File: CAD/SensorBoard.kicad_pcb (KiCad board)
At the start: 4 copper layers, 69.9 x 40 mm, 82 parts, among them J1 USB C 2.0, J2 SWD Connector, J3 UART Connector, J4 DAC Connector, M1 M1, M2 M2, M3 M3, M4 M4, SW1 SW_1, SW2 SW_2, SW3 SW_3, SW4 SW_4, SW5 SW_BOOT, SW6 SW_RST, U1 STM32U073CCT6, U2 MIC5365, U3 USBLC6-2SC6, U4 BME680, U5 BMI323, U6 TC1047, X1 32MHz, X2 32kHz768

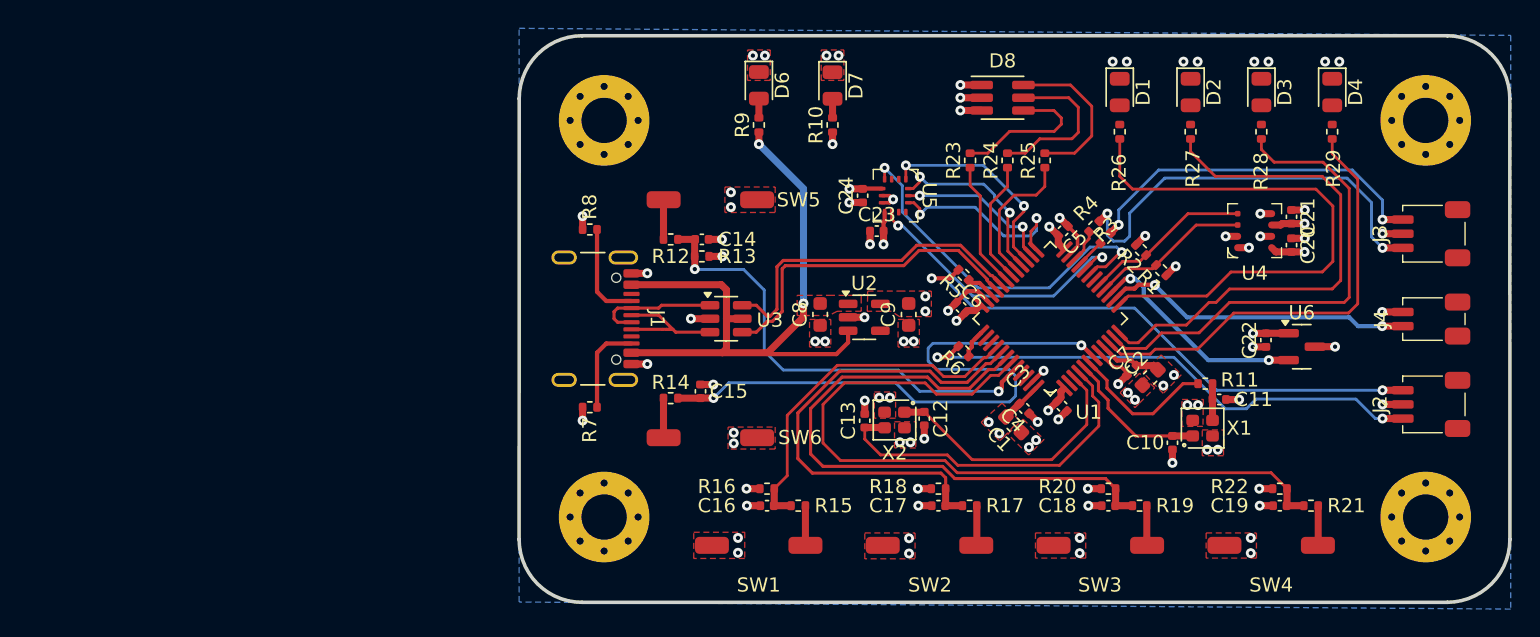
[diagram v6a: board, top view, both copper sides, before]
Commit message: Add initial silkscreen clean-up
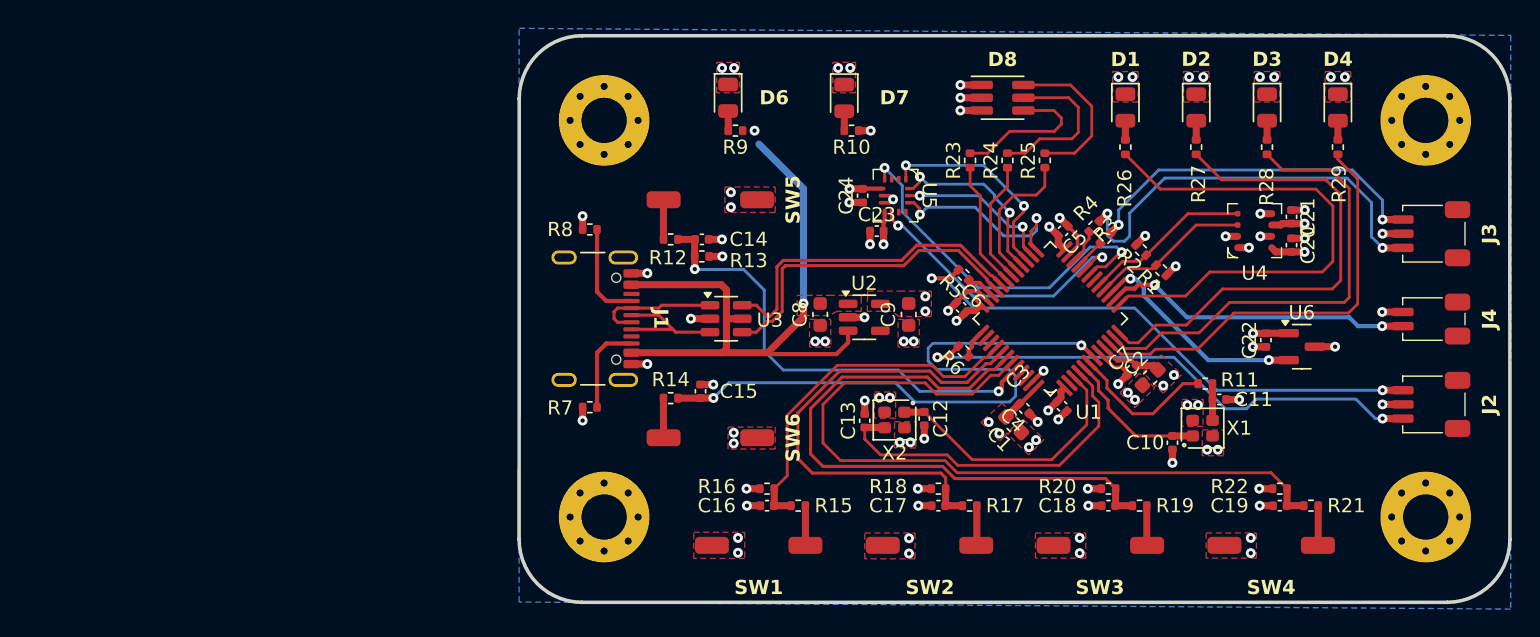
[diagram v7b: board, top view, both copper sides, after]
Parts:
- moved D6 2.35 mm to (137.2, 119.4)
- moved R9 1.71 mm to (137.8, 121.7), turned to 180 degrees
- moved R10 1.40 mm to (146.0, 121.7), turned to 180 degrees
- moved D7 1.20 mm to (145.4, 119.4)
- moved D1 1.16 mm to (165.3, 120.1)
- moved D2 1.16 mm to (170.3, 120.1)
- moved D3 1.16 mm to (175.3, 120.1)
- moved D4 1.16 mm to (180.3, 120.1)
- moved R26 1.16 mm to (165.3, 122.9)
- moved R27 1.16 mm to (170.3, 122.9)
- moved R28 1.16 mm to (175.3, 122.9)
- moved R29 1.16 mm to (180.3, 122.9)
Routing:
- net LED_1: track 38.8 -> 36.4 mm
- net LED_2: track 36.6 -> 35.2 mm
- net /LED_4_R: track 0.00 -> 1.35 mm
- net /LED_3_R: track 0.00 -> 1.35 mm
- net /LED_2_R: track 0.00 -> 1.35 mm
- net /LED_1_R: track 0.00 -> 1.35 mm
- net LED_3: track 34.1 -> 32.9 mm
- net LED_4: track 31.7 -> 30.5 mm
- net +5V: track 47.4 -> 46.5 mm

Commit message: Add keepout for sensors and clean silkscreen
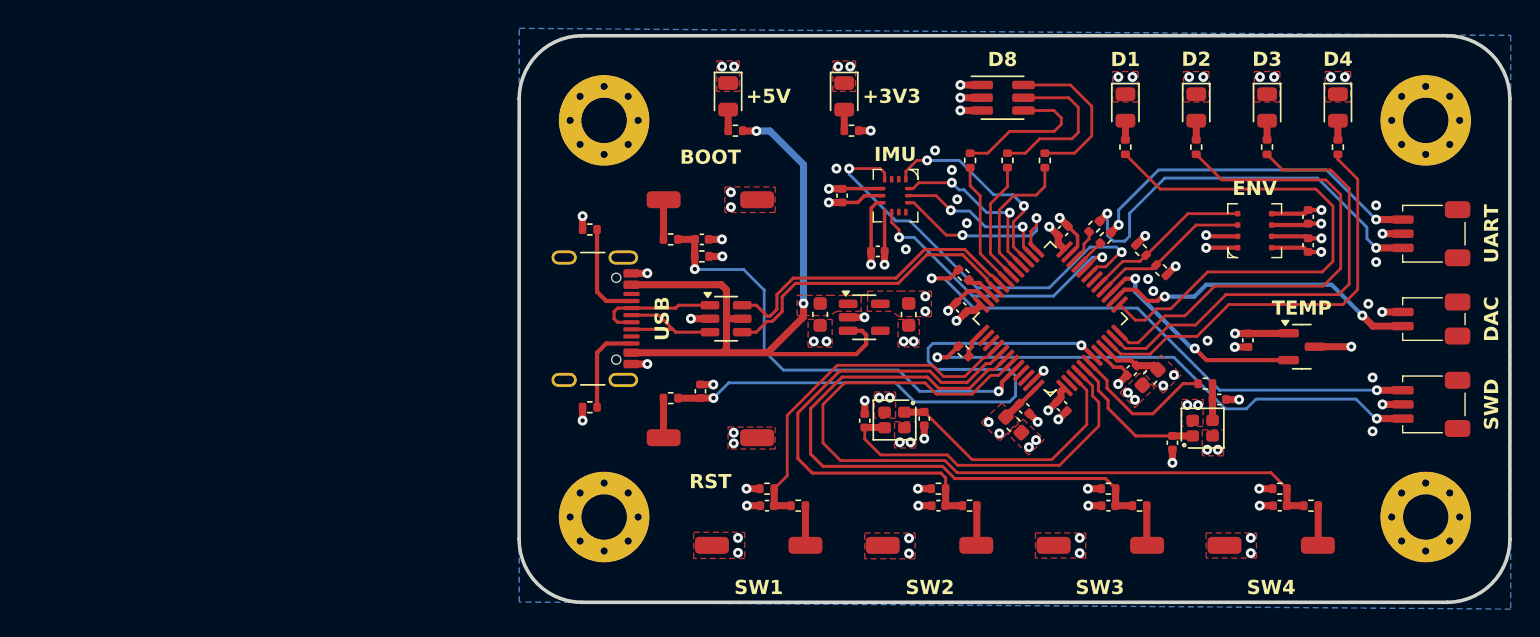
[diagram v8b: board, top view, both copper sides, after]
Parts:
- moved C24 1.45 mm to (145.3, 126.3)
- moved C23 1.43 mm to (147.8, 130.2)
- moved C22 1.27 mm to (173.9, 136.5)
- moved C20 1.17 mm to (178.2, 129.8)
- moved C21 1.17 mm to (178.2, 127.8)
- moved D7 0.12 mm to (145.4, 119.3)
- moved D6 0.10 mm to (137.2, 119.3)
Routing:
- net GND: track 53.5 -> 65.0 mm, vias 73 -> 84
- net +3V3: track 28.9 -> 36.9 mm
- net +5V: track 46.5 -> 51.5 mm
- net IMU_INT1: track 26.4 -> 30.3 mm
- net USB_D+: track 23.3 -> 21.9 mm
- net USB_D-: track 23.6 -> 22.2 mm
- net UART_RX: track 29.6 -> 28.7 mm
- net LED_1: track 36.4 -> 37.3 mm
- net UART_TX: track 25.3 -> 24.5 mm
- net SPI_NCS: track 14.3 -> 13.6 mm
- net SPI_MOSI: track 13.0 -> 12.3 mm
- net DAC_OUT: track 22.0 -> 22.6 mm
- net LED_4: track 30.5 -> 29.9 mm
- net LED_3: track 32.9 -> 32.3 mm
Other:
- board text added: "+3V3"
- board text added: "+5V"
- board text added: "BOOT"
- board text added: "DAC"
- board text added: "ENV"
- board text added: "IMU"
- board text added: "RST"
- board text added: "SWD"
- board text added: "TEMP"
- board text added: "UART"
- board text added: "USB"
